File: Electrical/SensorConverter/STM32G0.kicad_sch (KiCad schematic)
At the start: 16 parts, among them U3 AT24CS02-STUM, U7 STM32G0B1CEUx

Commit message: Finalized PCB RevB
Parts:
- removed C18: 100nF, Capacitor_SMD:C_0402_1005Metric, symbol Device:C
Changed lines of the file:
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@@
 	(paper "A4")
-	(junction
-		(at 53.34 129.54)
-		(diameter 0)
-		(color 0 0 0 0)
-	)
 	(junction
 		(at 200.66 73.66)
@@
 	)
 	(junction
-		(at 53.34 139.7)
-		(diameter 0)
-		(color 0 0 0 0)
-	)
-	(junction
 		(at 41.91 139.7)
 		(diameter 0)
@@
 	(wire
 		(pts
-			(xy 63.5 138.43) (xy 63.5 139.7)
-		)
-		(stroke
-			(width 0)
-			(type default)
-		)
-	)
-	(wire
-		(pts
 			(xy 177.8 55.88) (xy 180.34 55.88)
 		)
@@
 	(wire
 		(pts
-			(xy 53.34 139.7) (xy 63.5 139.7)
-		)
-		(stroke
-			(width 0)
-			(type default)
-		)
-	)
-	(wire
-		(pts
 			(xy 190.5 71.12) (xy 191.77 71.12)
 		)
@@
 	(wire
 		(pts
-			(xy 63.5 129.54) (xy 53.34 129.54)
-		)
-		(stroke
-			(width 0)
-			(type default)
-		)
-	)
-	(wire
-		(pts
 			(xy 177.8 76.2) (xy 180.34 76.2)
 		)
@@
 		(pts
 			(xy 41.91 138.43) (xy 41.91 139.7)
-		)
-		(stroke
-			(width 0)
-			(type default)
-		)
-	)
-	(wire
-		(pts
-			(xy 63.5 130.81) (xy 63.5 129.54)
 		)
 		(stroke
@@
 					(unit 1)
 				)
-			)
-		)
-	)
-	(symbol
-		(lib_id "Device:C")
-		(at 63.5 134.62 180)
-		(unit 1)
-		(exclude_from_sim no)
-		(in_bom yes)
-		(on_board yes)
-		(dnp no)
-		(property "Reference" "C18"
-			(at 67.31 133.35 0)
-			(effects
-				(font
-					(size 1.27 1.27)
-				)
-			)
-		)
-		(property "Value" "100nF"
-			(at 68.58 135.89 0)
-			(effects
-				(font
-					(size 1.27 1.27)
-				)
-			)
-		)
-		(property "Footprint" "Capacitor_SMD:C_0402_1005Metric"
-			(at 62.5348 130.81 0)
-			(effects
-				(font
-					(size 1.27 1.27)
-				)
-				(hide yes)
-			)
-		)
-		(property "Datasheet" "~"
-			(at 63.5 134.62 0)
-			(effects
-				(font
-					(size 1.27 1.27)
-				)
-				(hide yes)
-			)
-		)
-		(property "Description" ""
-			(at 63.5 134.62 0)
-			(effects
-				(font
-					(size 1.27 1.27)
-				)
-			)
-		)
-		(property "Voltage" "25V"
-			(at 63.5 134.62 0)
-			(effects
-				(font
-					(size 1.27 1.27)
-				)
-				(hide yes)
-			)
-		)
-		(pin "1"
-		)
-		(pin "2"
-		)
-		(instances
-			(project "SensorConverter"
-				(path "/6eed4ebc-b0cb-46ac-a470-b820c56ea840/46e8f11a-77d1-4418-9670-6e0d528a19bf"
-					(reference "C18")
-					(unit 1)
-				)

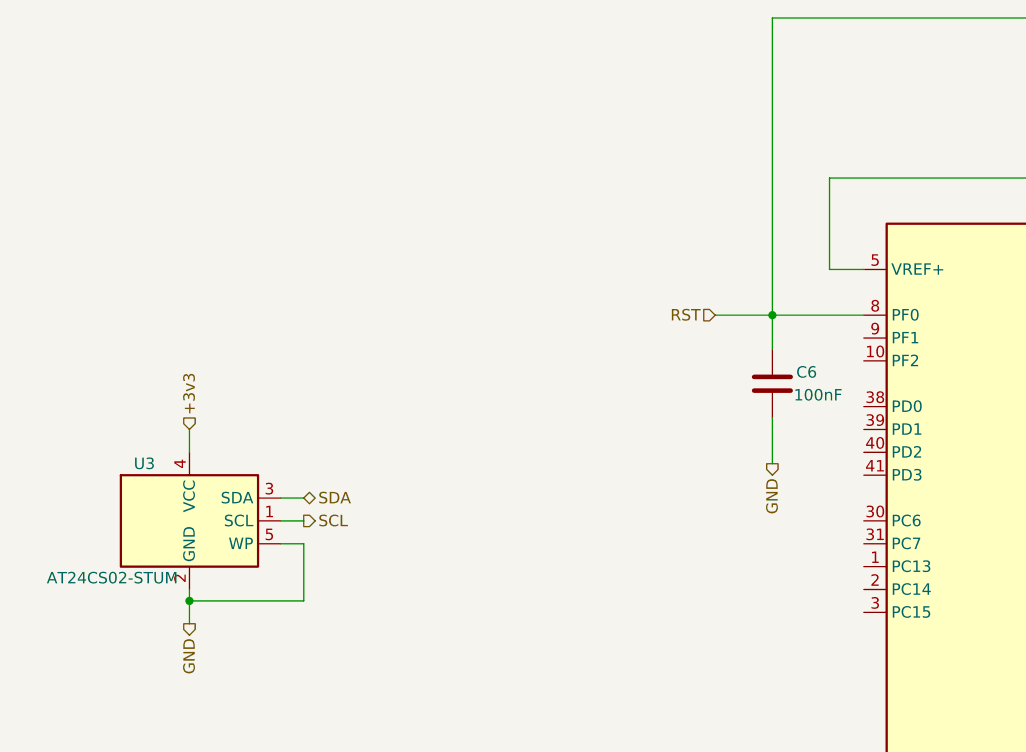
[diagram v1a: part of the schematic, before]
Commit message: Fixed minor changes in PCB
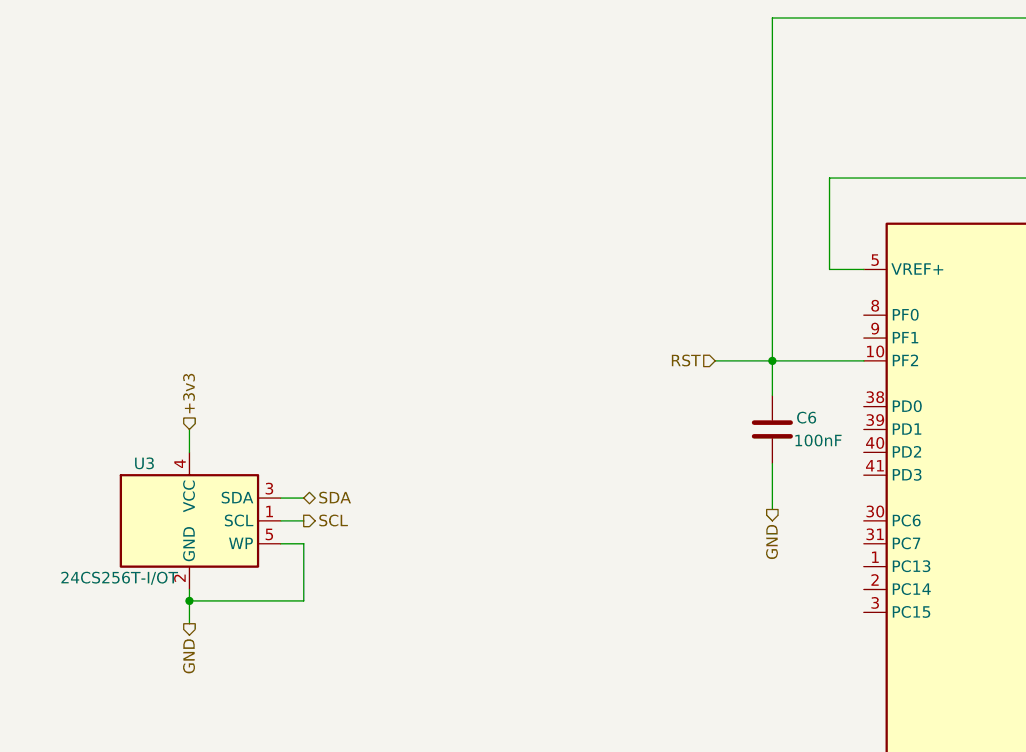
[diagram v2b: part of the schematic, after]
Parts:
- U3: value AT24CS02-STUM -> 24CS256T-I/OT
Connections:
- net RST: now also U7.10 (PF2); no longer U7.8 (PF0)
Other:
- moved on the sheet: C6
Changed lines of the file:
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@@
 	)
 	(junction
-		(at 111.76 53.34)
+		(at 111.76 58.42)
 		(diameter 0)
 		(color 0 0 0 0)
@@
 	(wire
 		(pts
-			(xy 111.76 53.34) (xy 111.76 57.15)
+			(xy 111.76 58.42) (xy 111.76 62.23)
 		)
 		(stroke
@@
 	(wire
 		(pts
-			(xy 111.76 53.34) (xy 121.92 53.34)
+			(xy 111.76 58.42) (xy 121.92 58.42)
 		)
 		(stroke
@@
 	(wire
 		(pts
-			(xy 105.41 53.34) (xy 111.76 53.34)
+			(xy 105.41 58.42) (xy 111.76 58.42)
 		)
 		(stroke
@@
 	(wire
 		(pts
-			(xy 111.76 20.32) (xy 111.76 53.34)
+			(xy 111.76 20.32) (xy 111.76 58.42)
 		)
 		(stroke
@@
 	(wire
 		(pts
-			(xy 111.76 64.77) (xy 111.76 69.85)
+			(xy 111.76 69.85) (xy 111.76 74.93)
 		)
 		(stroke
@@
 	(hierarchical_label "GND"
 		(shape output)
-		(at 111.76 69.85 270)
+		(at 111.76 74.93 270)
 		(effects
 			(font
@@
 	(hierarchical_label "RST"
 		(shape input)
-		(at 105.41 53.34 180)
+		(at 105.41 58.42 180)
 		(effects
 			(font
@@
 			)
 		)
-		(property "Value" "AT24CS02-STUM"
+		(property "Value" "24CS256T-I/OT"
 			(at 45.72 82.55 0)
 			(effects
@@
 	(symbol
 		(lib_id "Device:C")
-		(at 111.76 60.96 180)
+		(at 111.76 66.04 180)
 		(unit 1)
 		(exclude_from_sim no)
@@
 		(dnp no)
 		(property "Reference" "C6"
-			(at 115.57 59.69 0)
+			(at 115.57 64.77 0)
 			(effects
 				(font
@@
 		)
 		(property "Value" "100nF"
-			(at 116.84 62.23 0)
+			(at 116.84 67.31 0)
 			(effects
 				(font
@@
 		)
 		(property "Footprint" "Capacitor_SMD:C_0402_1005Metric"
-			(at 110.7948 57.15 0)
+			(at 110.7948 62.23 0)
 			(effects
 				(font
@@
 		)
 		(property "Datasheet" "~"
-			(at 111.76 60.96 0)
+			(at 111.76 66.04 0)
 			(effects
 				(font
@@
 		)
 		(property "Description" ""
-			(at 111.76 60.96 0)
+			(at 111.76 66.04 0)
 			(effects
 				(font
@@
 		)
 		(property "Voltage" "25V"
-			(at 111.76 60.96 0)
-			(effects
-				(font
+			(at 111.76 66.04 0)
+			(effects
+				(font

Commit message: WIP
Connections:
- net SCL: now also U7.45 (PB6); no longer U7.33 (PA9/PA11)
- net SDA: now also U7.46 (PB7); no longer U7.29 (PA9/UCPD1_DBCC1)
- net USART1_RX: now also U7.32 (PA10/UCPD1_DBCC2); no longer U7.45 (PB6)
- net USART1_TX: now also U7.29 (PA9/UCPD1_DBCC1); no longer U7.46 (PB7)
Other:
- moved on the sheet: R4, R5
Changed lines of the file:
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@@
 	(paper "A4")
 	(junction
-		(at 200.66 73.66)
+		(at 266.7 109.22)
 		(diameter 0)
 		(color 0 0 0 0)
@@
 	)
 	(junction
-		(at 190.5 71.12)
+		(at 256.54 106.68)
 		(diameter 0)
 		(color 0 0 0 0)
@@
 	)
 	(junction
-		(at 195.58 59.69)
+		(at 261.62 95.25)
 		(diameter 0)
 		(color 0 0 0 0)
@@
 	(wire
 		(pts
-			(xy 177.8 109.22) (xy 180.34 109.22)
-		)
-		(stroke
-			(width 0)
-			(type default)
-		)
-	)
-	(wire
-		(pts
-			(xy 200.66 73.66) (xy 200.66 68.58)
+			(xy 177.8 109.22) (xy 266.7 109.22)
+		)
+		(stroke
+			(width 0)
+			(type default)
+		)
+	)
+	(wire
+		(pts
+			(xy 177.8 73.66) (xy 180.34 73.66)
+		)
+		(stroke
+			(width 0)
+			(type default)
+		)
+	)
+	(wire
+		(pts
+			(xy 266.7 109.22) (xy 266.7 104.14)
 		)
 		(stroke
@@
 	(wire
 		(pts
-			(xy 195.58 58.42) (xy 195.58 59.69)
+			(xy 261.62 93.98) (xy 261.62 95.25)
 		)
 		(stroke
@@
 	(wire
 		(pts
-			(xy 190.5 71.12) (xy 191.77 71.12)
+			(xy 256.54 106.68) (xy 257.81 106.68)
 		)
 		(stroke
@@
 	(wire
 		(pts
-			(xy 200.66 60.96) (xy 200.66 59.69)
+			(xy 266.7 96.52) (xy 266.7 95.25)
 		)
 		(stroke
@@
 	(wire
 		(pts
-			(xy 200.66 73.66) (xy 203.2 73.66)
+			(xy 266.7 109.22) (xy 269.24 109.22)
 		)
 		(stroke
@@
 	(wire
 		(pts
-			(xy 177.8 73.66) (xy 200.66 73.66)
-		)
-		(stroke
-			(width 0)
-			(type default)
-		)
-	)
-	(wire
-		(pts
 			(xy 240.03 127) (xy 240.03 142.24)
 		)
@@
 	(wire
 		(pts
-			(xy 200.66 59.69) (xy 195.58 59.69)
+			(xy 266.7 95.25) (xy 261.62 95.25)
 		)
 		(stroke
@@
 	(wire
 		(pts
-			(xy 111.76 20.32) (xy 111.76 58.42)
-		)
-		(stroke
-			(width 0)
-			(type default)
-		)
-	)
-	(wire
-		(pts
-			(xy 250.19 20.32) (xy 111.76 20.32)
-		)
-		(stroke
-			(width 0)
-			(type default)
-		)
-	)
-	(wire
-		(pts
 			(xy 215.9 127) (xy 240.03 127)
 		)
@@
 	(wire
 		(pts
-			(xy 177.8 106.68) (xy 180.34 106.68)
-		)
-		(stroke
-			(width 0)
-			(type default)
-		)
-	)
-	(wire
-		(pts
-			(xy 190.5 60.96) (xy 190.5 59.69)
+			(xy 177.8 78.74) (xy 180.34 78.74)
+		)
+		(stroke
+			(width 0)
+			(type default)
+		)
+	)
+	(wire
+		(pts
+			(xy 177.8 106.68) (xy 256.54 106.68)
+		)
+		(stroke
+			(width 0)
+			(type default)
+		)
+	)
+	(wire
+		(pts
+			(xy 256.54 96.52) (xy 256.54 95.25)
 		)
 		(stroke
@@
 	(wire
 		(pts
-			(xy 195.58 59.69) (xy 190.5 59.69)
+			(xy 261.62 95.25) (xy 256.54 95.25)
 		)
 		(stroke
@@
 	(wire
 		(pts
-			(xy 177.8 71.12) (xy 190.5 71.12)
-		)
-		(stroke
-			(width 0)
-			(type default)
-		)
-	)
-	(wire
-		(pts
 			(xy 177.8 83.82) (xy 180.34 83.82)
 		)
@@
 	(wire
 		(pts
-			(xy 190.5 68.58) (xy 190.5 71.12)
+			(xy 256.54 104.14) (xy 256.54 106.68)
 		)
 		(stroke
@@
 	(hierarchical_label "SCL"
 		(shape output)
-		(at 191.77 71.12 0)
+		(at 257.81 106.68 0)
 		(effects
 			(font
@@
 	(hierarchical_label "SDA"
 		(shape bidirectional)
-		(at 203.2 73.66 0)
+		(at 269.24 109.22 0)
 		(effects
 			(font
@@
 	(hierarchical_label "USART1_TX"
 		(shape output)
-		(at 180.34 109.22 0)
+		(at 180.34 73.66 0)
 		(effects
 			(font
@@
 	(hierarchical_label "USART1_RX"
 		(shape input)
-		(at 180.34 106.68 0)
+		(at 180.34 78.74 0)
 		(effects
 			(font
@@
 	(hierarchical_label "+3v3"
 		(shape input)
-		(at 195.58 58.42 90)
+		(at 261.62 93.98 90)
 		(effects
 			(font
@@
 	(symbol
 		(lib_id "Device:R")
-		(at 200.66 64.77 0)
+		(at 266.7 100.33 0)
 		(mirror y)
 		(unit 1)
@@
 		(fields_autoplaced yes)
 		(property "Reference" "R4"
-			(at 198.12 63.4999 0)
+			(at 264.16 99.0599 0)
 			(effects
 				(font
@@
 		)
 		(property "Value" "10k"
-			(at 198.12 66.0399 0)
+			(at 264.16 101.5999 0)
 			(effects
 				(font
@@
 		)
 		(property "Footprint" "Resistor_SMD:R_0402_1005Metric"
-			(at 202.438 64.77 90)
+			(at 268.478 100.33 90)
 			(effects
 				(font
@@
 		)
 		(property "Datasheet" "~"
-			(at 200.66 64.77 0)
+			(at 266.7 100.33 0)
 			(effects
 				(font
@@
 		)
 		(property "Description" ""
-			(at 200.66 64.77 0)
+			(at 266.7 100.33 0)
 			(effects
 				(font
@@
 	(symbol
 		(lib_id "Device:R")
-		(at 190.5 64.77 0)
+		(at 256.54 100.33 0)
 		(mirror y)
 		(unit 1)
@@
 		(fields_autoplaced yes)
 		(property "Reference" "R5"
-			(at 187.96 63.4999 0)
+			(at 254 99.0599 0)
 			(effects
 				(font
@@
 		)
 		(property "Value" "10k"
-			(at 187.96 66.0399 0)
+			(at 254 101.5999 0)
 			(effects
 				(font
@@
 		)
 		(property "Footprint" "Resistor_SMD:R_0402_1005Metric"
-			(at 192.278 64.77 90)
+			(at 258.318 100.33 90)
 			(effects
 				(font
@@
 		)
 		(property "Datasheet" "~"
-			(at 190.5 64.77 0)
+			(at 256.54 100.33 0)
 			(effects
 				(font
@@
 		)
 		(property "Description" ""
-			(at 190.5 64.77 0)
-			(effects
-				(font
+			(at 256.54 100.33 0)
+			(effects
+				(font
